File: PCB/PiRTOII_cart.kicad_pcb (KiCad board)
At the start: 2 copper layers, 58.2 x 77.5 mm, 15 parts, among them CN1 EDGE_CONN, CN2 MICRO_SD_SLOT, J1 CONN_SNOOP, Q1 BC547, SW1 BTN_RESET_PICO, U1 PICO, U2 74LVC245, U3 74LVC245, U4 74LVC245

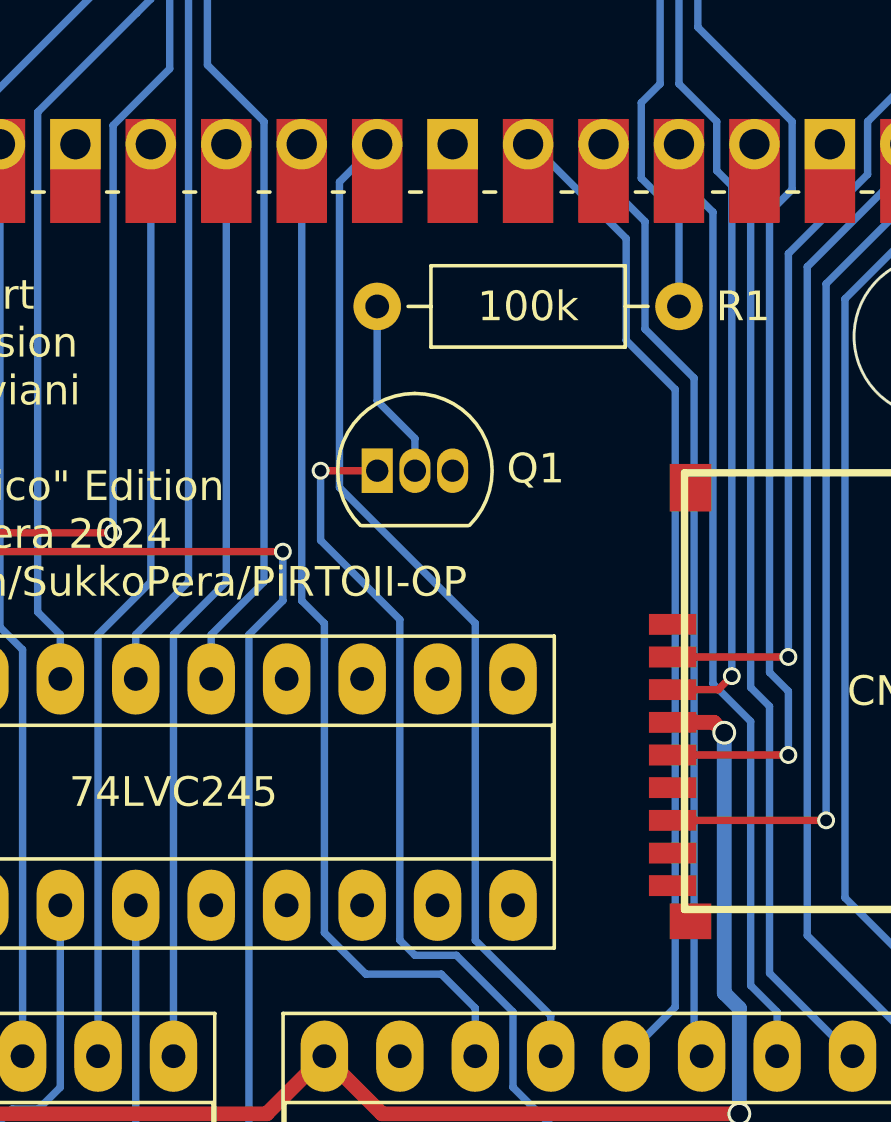
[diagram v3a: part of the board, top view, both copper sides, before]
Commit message: Use better BJT footprint
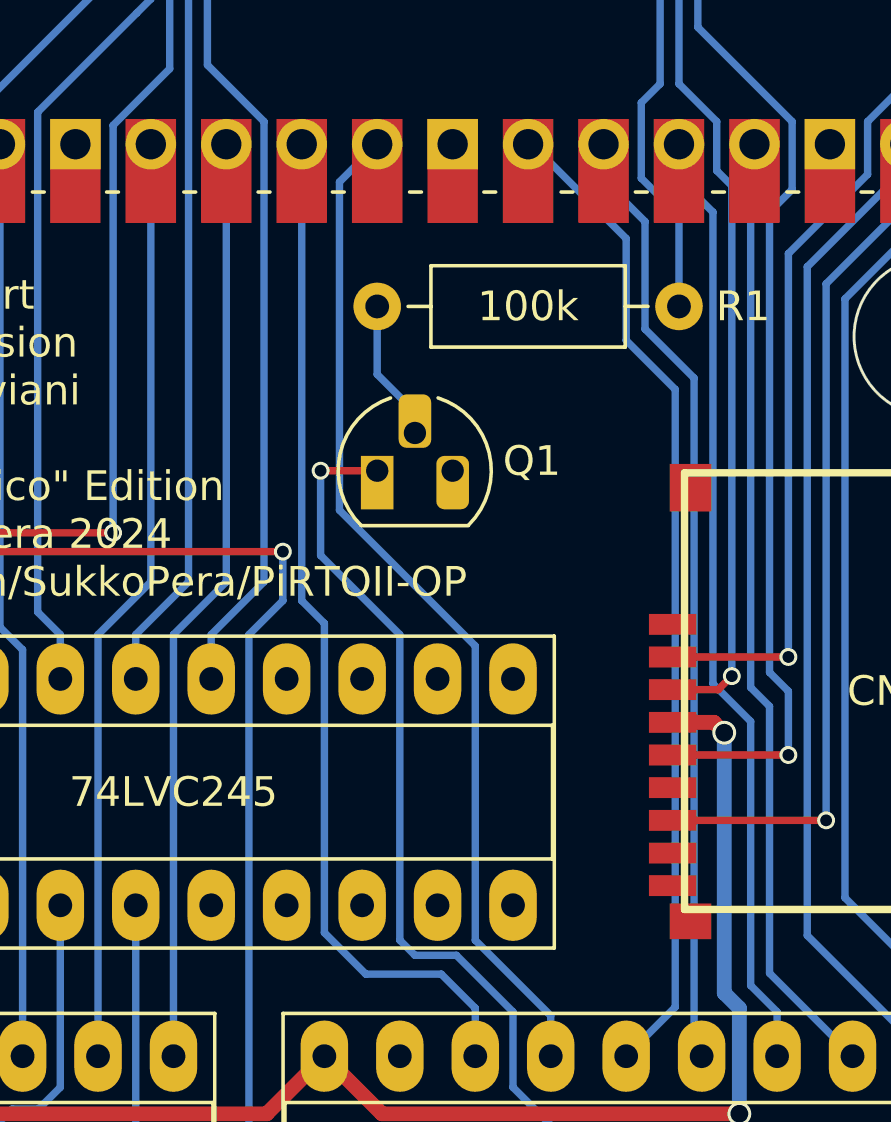
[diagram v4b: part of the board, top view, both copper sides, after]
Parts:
- Q1: footprint Package_TO_SOT_THT:TO-92_Inline -> Package_TO_SOT_THT:TO-92_HandSolder
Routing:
- net Net-(Q1-B): track 6.06 -> 4.08 mm
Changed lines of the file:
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@@
 		)
 	)
-	(footprint "Package_TO_SOT_THT:TO-92_Inline"
+	(footprint "Package_TO_SOT_THT:TO-92_HandSolder"
 		(layer "F.Cu")
 		(at 122.301 139.515)
-		(descr "TO-92 leads in-line, narrow, oval pads, drill 0.75mm (see NXP sot054_po.pdf)")
+		(descr "TO-92 leads molded, narrow, drill 0.75mm, handsoldering variant with enlarged pads (see NXP sot054_po.pdf)")
 		(tags "to-92 sc-43 sc-43a sot54 PA33 transistor")
 		(property "Reference" "Q1"
-			(at 5.334 -0.069 180)
+			(at 5.207 -0.323 0)
 			(layer "F.SilkS")
 			(effects
@@
 			)
 		)
-		(property "Footprint" "Package_TO_SOT_THT:TO-92_Inline"
+		(property "Footprint" "Package_TO_SOT_THT:TO-92_HandSolder"
 			(at 0 0 0)
 			(unlocked yes)
@@
 		)
 		(fp_arc
-			(start -0.568478 1.838478)
-			(mid -1.132087 -0.994977)
-			(end 1.27 -2.6)
+			(start -0.541875 1.841741)
+			(mid -1.247231 -0.581764)
+			(end 0.45 -2.45)
 			(stroke
 				(width 0.12)
@@
 		)
 		(fp_arc
-			(start 1.27 -2.6)
-			(mid 3.672087 -0.994977)
-			(end 3.108478 1.838478)
+			(start 2.05 -2.45)
+			(mid 3.769931 -0.601036)
+			(end 3.078445 1.827684)
 			(stroke
 				(width 0.12)
@@
 		)
 		(fp_line
-			(start -1.46 -2.73)
+			(start -1.46 -3.05)
 			(end -1.46 2.01)
 			(stroke
@@
 		)
 		(fp_line
-			(start -1.46 -2.73)
-			(end 4 -2.73)
+			(start -1.46 -3.05)
+			(end 4 -3.05)
 			(stroke
 				(width 0.05)
@@
 		(fp_line
 			(start 4 2.01)
-			(end 4 -2.73)
+			(end 4 -3.05)
 			(stroke
 				(width 0.05)
@@
 		(pad "1" thru_hole rect
 			(at 0 0)
-			(size 1.05 1.5)
-			(drill 0.75)
+			(size 1.1 1.8)
+			(drill 0.75
+				(offset 0 0.4)
+			)
 			(layers "*.Cu" "*.Mask")
 			(remove_unused_layers no)
@@
 			(pintype "passive")
 		)
-		(pad "2" thru_hole oval
-			(at 1.27 0)
-			(size 1.05 1.5)
-			(drill 0.75)
+		(pad "2" thru_hole roundrect
+			(at 1.27 -1.27)
+			(size 1.1 1.8)
+			(drill 0.75
+				(offset 0 -0.4)
+			)
 			(layers "*.Cu" "*.Mask")
 			(remove_unused_layers no)
+			(roundrect_rratio 0.25)
 			(net 56 "Net-(Q1-B)")
 			(pinfunction "B")
 			(pintype "input")
 		)
-		(pad "3" thru_hole oval
+		(pad "3" thru_hole roundrect
 			(at 2.54 0)
-			(size 1.05 1.5)
-			(drill 0.75)
+			(size 1.1 1.8)
+			(drill 0.75
+				(offset 0 0.4)
+			)
 			(layers "*.Cu" "*.Mask")
 			(remove_unused_layers no)
+			(roundrect_rratio 0.25)
 			(net 2 "GND")
 			(pinfunction "E")
 			(pintype "passive")
 		)
-		(model "${KICAD8_3DMODEL_DIR}/Package_TO_SOT_THT.3dshapes/TO-92_Inline.wrl"
+		(model "${KICAD8_3DMODEL_DIR}/Package_TO_SOT_THT.3dshapes/TO-92.wrl"
 			(offset
 				(xyz 0 0 0)
@@
 	)
 	(segment
-		(start 130.683 172.466)
-		(end 130.683 173.99)
+		(start 120.396 142.367)
+		(end 123.063 145.034)
 		(width 0.25)
 		(layer "B.Cu")
@@
 	)
 	(segment
-		(start 129.413 162.814)
-		(end 129.413 171.196)
+		(start 126.873 160.274)
+		(end 129.413 162.814)
 		(width 0.25)
 		(layer "B.Cu")
@@
 	)
 	(segment
-		(start 130.683 173.99)
-		(end 131.953 175.26)
+		(start 120.396 139.515)
+		(end 120.396 142.367)
 		(width 0.25)
 		(layer "B.Cu")
@@
 	)
 	(segment
-		(start 126.873 160.274)
-		(end 129.413 162.814)
+		(start 130.683 172.466)
+		(end 130.683 173.99)
 		(width 0.25)
 		(layer "B.Cu")
@@
 	)
 	(segment
-		(start 120.396 139.515)
-		(end 120.396 141.859)
+		(start 124.968 155.829)
+		(end 126.873 157.734)
 		(width 0.25)
 		(layer "B.Cu")
@@
 	)
 	(segment
-		(start 123.063 155.321)
-		(end 123.571 155.829)
+		(start 123.063 145.034)
+		(end 123.063 155.321)
 		(width 0.25)
 		(layer "B.Cu")
@@
 	)
 	(segment
-		(start 120.396 141.859)
-		(end 123.063 144.526)
+		(start 123.063 155.321)
+		(end 123.571 155.829)
 		(width 0.25)
 		(layer "B.Cu")
@@
 	)
 	(segment
-		(start 123.571 155.829)
-		(end 124.968 155.829)
+		(start 130.683 173.99)
+		(end 131.953 175.26)
 		(width 0.25)
 		(layer "B.Cu")
@@
 	)
 	(segment
-		(start 123.063 144.526)
-		(end 123.063 155.321)
+		(start 129.413 171.196)
+		(end 130.683 172.466)
 		(width 0.25)
 		(layer "B.Cu")
@@
 	)
 	(segment
-		(start 124.968 155.829)
-		(end 126.873 157.734)
+		(start 123.571 155.829)
+		(end 124.968 155.829)
 		(width 0.25)
 		(layer "B.Cu")
@@
 	)
 	(segment
-		(start 129.413 171.196)
-		(end 130.683 172.466)
+		(start 131.953 175.735)
+		(end 131.953 175.006)
 		(width 0.25)
 		(layer "B.Cu")
@@
 	)
 	(segment
-		(start 131.953 175.735)
-		(end 131.953 175.006)
+		(start 129.413 162.814)
+		(end 129.413 171.196)
 		(width 0.25)
 		(layer "B.Cu")
@@
 	)
 	(segment
-		(start 122.301 133.985)
-		(end 122.301 137.16)
-		(width 0.25)
-		(layer "B.Cu")
-		(net 56)
-	)
-	(segment
-		(start 123.571 138.43)
-		(end 123.571 139.515)
+		(start 122.301 136.271)
+		(end 123.571 137.541)
 		(width 0.25)
 		(layer "B.Cu")
@@
 	)
 	(segment
-		(start 122.301 137.16)
-		(end 123.571 138.43)
+		(start 122.301 133.985)
+		(end 122.301 136.271)
 		(width 0.25)
 		(layer "B.Cu")
@@
 	)
 	(segment
-		(start 125.603 144.653)
-		(end 125.603 155.321)
+		(start 121.031 129.794)
+		(end 121.031 140.843)
 		(width 0.25)
 		(layer "B.Cu")
@@
 	)
 	(segment
-		(start 121.031 129.794)
-		(end 121.031 140.081)
+		(start 128.143 157.861)
+		(end 128.143 159.225)
 		(width 0.25)
 		(layer "B.Cu")
@@
 	)
 	(segment
-		(start 121.031 140.081)
-		(end 125.603 144.653)
+		(start 125.603 145.415)
+		(end 125.603 155.321)
 		(width 0.25)
 		(layer "B.Cu")
@@
 	)
 	(segment
-		(start 128.143 157.861)
-		(end 128.143 159.225)
+		(start 121.031 140.843)
+		(end 125.603 145.415)
 		(width 0.25)
 		(layer "B.Cu")
@@
 		(name "$teardrop_track$")
 		(hatch full 0.1)
-		(priority 30002)
+		(priority 30001)
 		(attr
 			(teardrop
@@
 		(name "$teardrop_track$")
 		(hatch full 0.1)
-		(priority 30003)
+		(priority 30004)
 		(attr
 			(teardrop
@@
 		(polygon
 			(pts
-				(xy 103.451 129.167) (xy 103.051 129.167) (xy 103.001 129.667) (xy 103.251 129.668) (xy 103.501 129.667)
+				(xy 103.051 128.135) (xy 103.451 128.135) (xy 103.501 127.635) (xy 103.251 127.634) (xy 103.001 127.635)
 			)
 		)
@@
 	)
 	(zone
+		(net 0)
+		(net_name "")
+		(layer "B.Cu")
+		(hatch edge 0.5)
+		(connect_pads
+			(clearance 0)
+		)
+		(min_thickness 0.25)
+		(filled_areas_thickness no)
+		(keepout
+			(tracks allowed)
+			(vias allowed)
+			(pads allowed)
+			(copperpour not_allowed)
+			(footprints allowed)
+		)
+		(fill
+			(thermal_gap 0.5)
+			(thermal_bridge_width 0.5)
+		)
+		(polygon
+			(pts
+				(xy 111.379 127.381) (xy 112.903 127.381) (xy 112.903 129.921) (xy 111.379 129.921)
+			)
+		)
+	)
+	(zone
 		(net 1)
 		(net_name "+5V")
@@
 		(name "$teardrop_track$")
 		(hatch full 0.1)
-		(priority 30001)
+		(priority 30000)
 		(attr
 			(teardrop
@@
 		(polygon
 			(pts
-				(xy 92.383 174.965) (xy 92.783 174.965) (xy 92.833 174.465) (xy 92.583 174.464) (xy 92.333 174.465)
+				(xy 92.783 176.284) (xy 92.383 176.284) (xy 92.333 176.784) (xy 92.583 176.785) (xy 92.833 176.784)
 			)
 		)
 	)
 	(zone
-		(net 0)
-		(net_name "")
+		(net 63)
+		(net_name "+3.3V")
 		(layer "B.Cu")
-		(hatch edge 0.5)
-		(connect_pads
+		(name "$teardrop_track$")
+		(hatch full 0.1)
+		(priority 30003)
+		(attr
+			(teardrop
+				(type track_end)
+			)
+		)
+		(connect_pads yes
 			(clearance 0)
 		)
-		(min_thickness 0.25)
+		(min_thickness 0.0254)
 		(filled_areas_thickness no)
-		(keepout
-			(tracks allowed)
-			(vias allowed)
-			(pads allowed)
-			(copperpour not_allowed)
-			(footprints allowed)
-		)
-		(fill
+		(fill yes
 			(thermal_gap 0.5)
 			(thermal_bridge_width 0.5)
+			(island_removal_mode 1)
+			(island_area_min 10)
 		)
 		(polygon
 			(pts
-				(xy 111.379 127.381) (xy 112.903 127.381) (xy 112.903 129.921) (xy 111.379 129.921)
+				(xy 103.451 129.167) (xy 103.051 129.167) (xy 103.001 129.667) (xy 103.251 129.668) (xy 103.501 129.667)
 			)
 		)
@@
 		(name "$teardrop_track$")
 		(hatch full 0.1)
-		(priority 30000)
+		(priority 30002)
 		(attr
 			(teardrop
@@
 		(polygon
 			(pts
-				(xy 92.783 176.284) (xy 92.383 176.284) (xy 92.333 176.784) (xy 92.583 176.785) (xy 92.833 176.784)
+				(xy 92.383 174.965) (xy 92.783 174.965) (xy 92.833 174.465) (xy 92.583 174.464) (xy 92.333 174.465)
 			)
 		)
@@
 			)
 		)
-	)
-	(zone
-		(net 63)
-		(net_name "+3.3V")
-		(layer "B.Cu")
-		(name "$teardrop_track$")
-		(hatch full 0.1)
-		(priority 30004)
-		(attr
-			(teardrop
-				(type track_end)
-			)
-		)
-		(connect_pads yes
-			(clearance 0)
-		)
-		(min_thickness 0.0254)
-		(filled_areas_thickness no)
-		(fill yes
-			(thermal_gap 0.5)
-			(thermal_bridge_width 0.5)
-			(island_removal_mode 1)
-			(island_area_min 10)
-		)
-		(polygon
-			(pts
-				(xy 103.051 128.135) (xy 103.451 128.135) (xy 103.501 127.635) (xy 103.251 127.634) (xy 103.001 127.635)
-			)
-		)

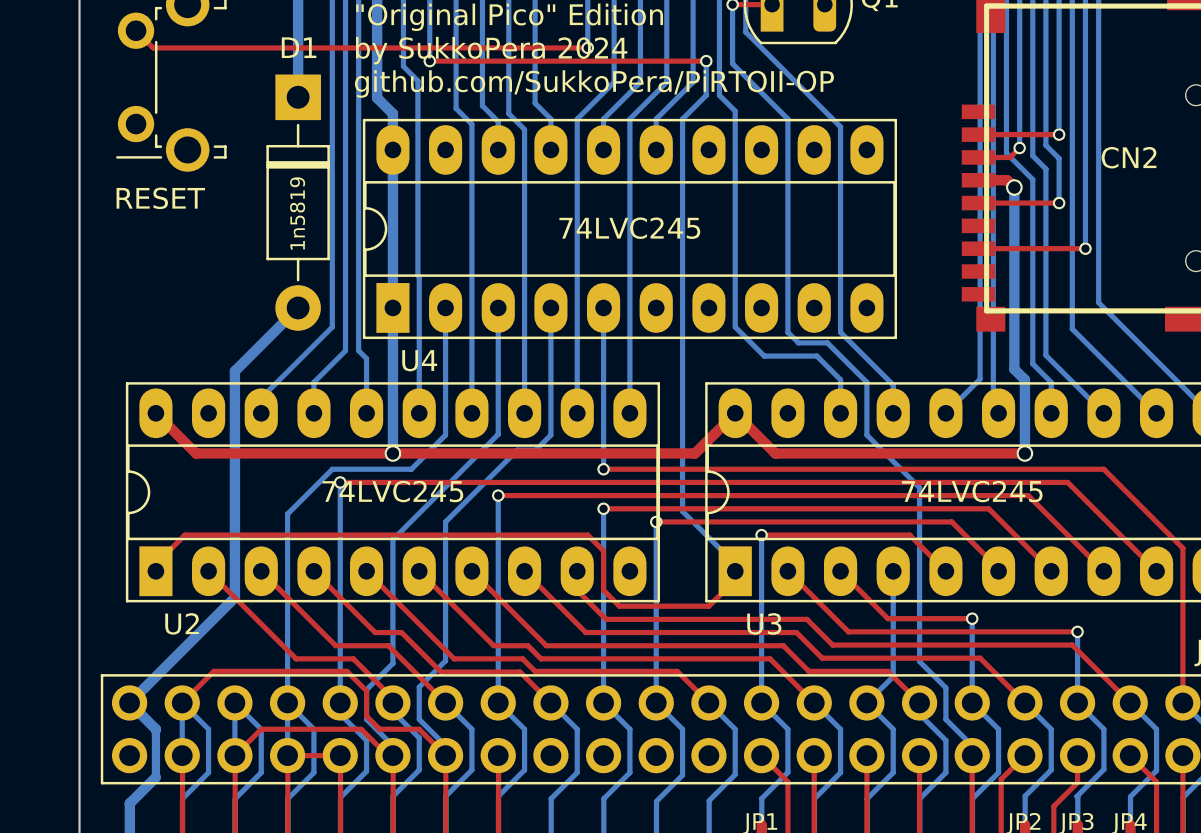
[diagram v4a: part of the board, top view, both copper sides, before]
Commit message: Add SD slot signal labels (?)
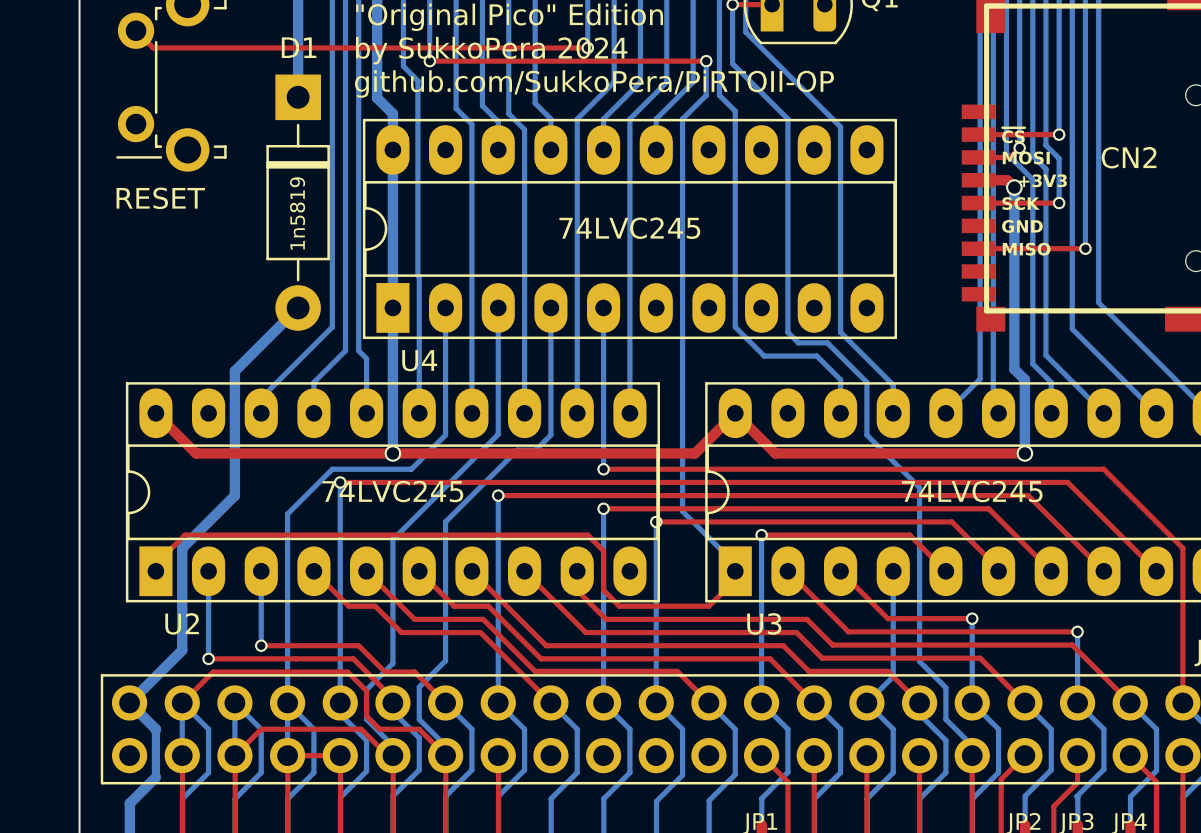
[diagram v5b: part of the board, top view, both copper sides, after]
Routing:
- net d0': track 26.8 -> 29.3 mm, vias 0 -> 1
- net d1': track 27.3 -> 29.4 mm, vias 0 -> 1
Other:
- board text added: "+3V3"
- board text added: "MISO"
- board text added: "MOSI"
- board text added: "SCK"
- board text added: "~{CS}"

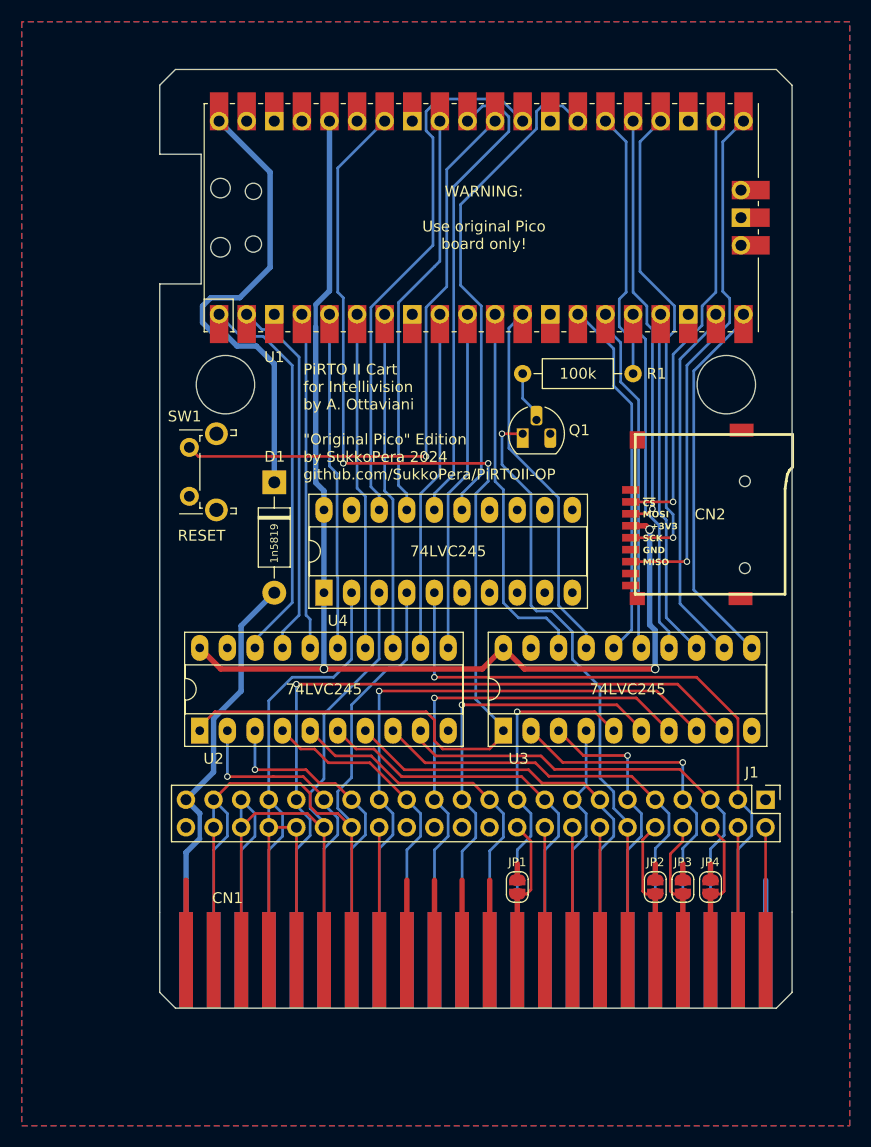
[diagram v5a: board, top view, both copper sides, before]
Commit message: Use the two BC1/2/BDIR sets more properly
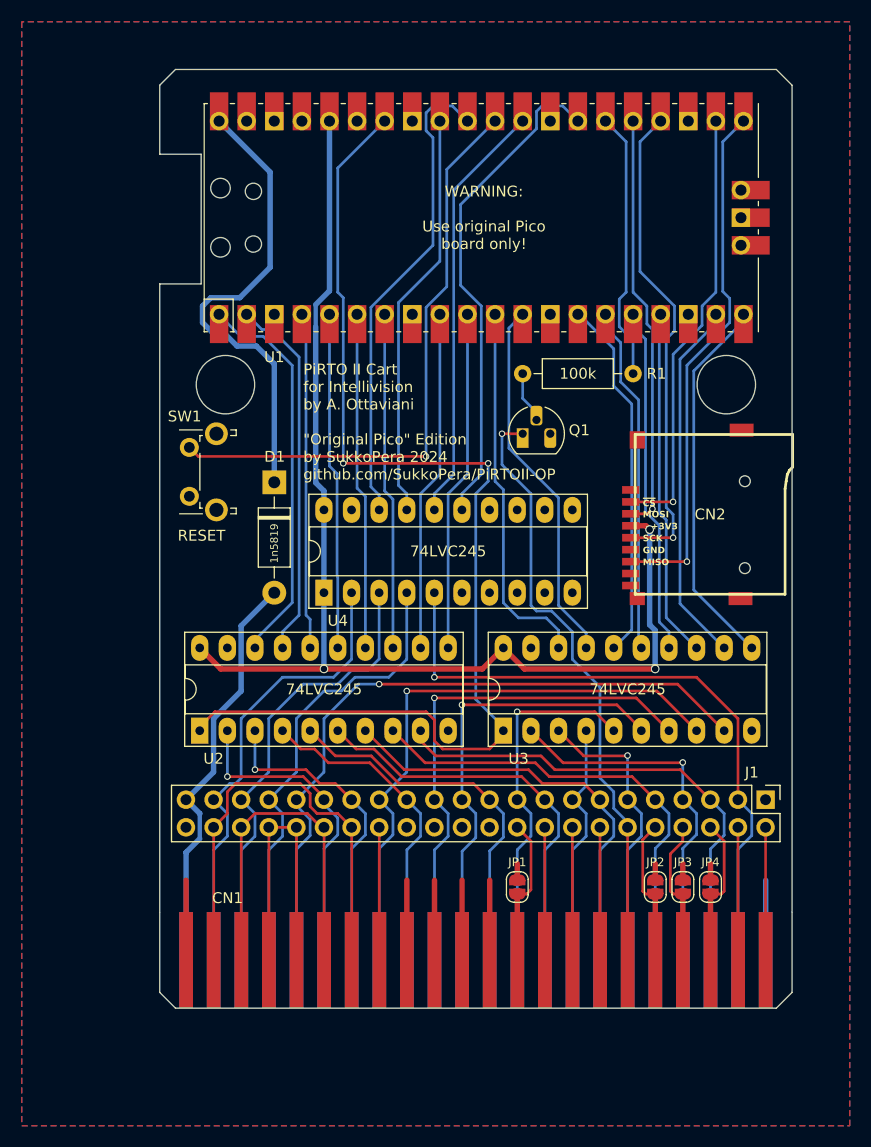
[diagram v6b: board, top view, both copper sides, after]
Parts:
- CN2: value MICRO_SD_SLOT -> MICRO_SD_SLOT
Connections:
- CN1 pad 32: bc1' -> /bc1_in
- CN1 pad 34: bc2' -> /bc2_in
- CN1 pad 36: bdir' -> /bdir_in
- CN1 pad 38: bdir' -> /bdir_in
- CN1 pad 40: bc2' -> /bc2_in
- CN1 pad 42: bc1' -> /bc1_in
- J1 pad 32: bc1' -> /bc1_in
- J1 pad 34: bc2' -> /bc2_in
- J1 pad 36: bdir' -> /bdir_in
- J1 pad 38: bdir' -> /bdir_in
- J1 pad 40: bc2' -> /bc2_in
- J1 pad 42: bc1' -> /bc1_in
- U4 pad 16: bc1_lv -> bdir_lv
- U4 pad 18: bdir_lv -> bc1_lv
- U4 pad 2: bdir' -> bc1'
- U4 pad 4: bc1' -> bdir'
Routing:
- net /bc1_in: track 0.00 -> 42.3 mm
- net bc1': track 83.3 -> 43.2 mm
- net /bc2_in: track 0.00 -> 32.8 mm
- net bc2': track 75.5 -> 42.9 mm
- net /bdir_in: track 0.00 -> 27.0 mm
- net bdir': track 69.8 -> 42.9 mm
- net bdir_lv: track 49.8 -> 39.1 mm
- net d15': track 67.1 -> 63.7 mm
- net d14': track 56.6 -> 55.0 mm
- net d11_lv: track 32.1 -> 31.1 mm
- net d0_lv: track 36.1 -> 35.4 mm
- net d15_lv: track 34.8 -> 34.2 mm
